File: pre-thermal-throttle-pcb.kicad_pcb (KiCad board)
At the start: 2 copper layers, 101.6 x 89.5 mm, 62 parts, among them IC1 LMR51420XFDDCR, IC2 ADR02BRZ-REEL7, IC3 ADR02BRZ-REEL7, IC4 ADR02BRZ-REEL7, IC5 ADR02BRZ-REEL7, J1 RJHSE-5381-ND, J2 STEERING, J3 Motor Throttle Connector, U1 SN65HVD230, U2 BMI088, U3 MAX3485CSA, U4 MCP3008, U5 ESP32-DevKitC

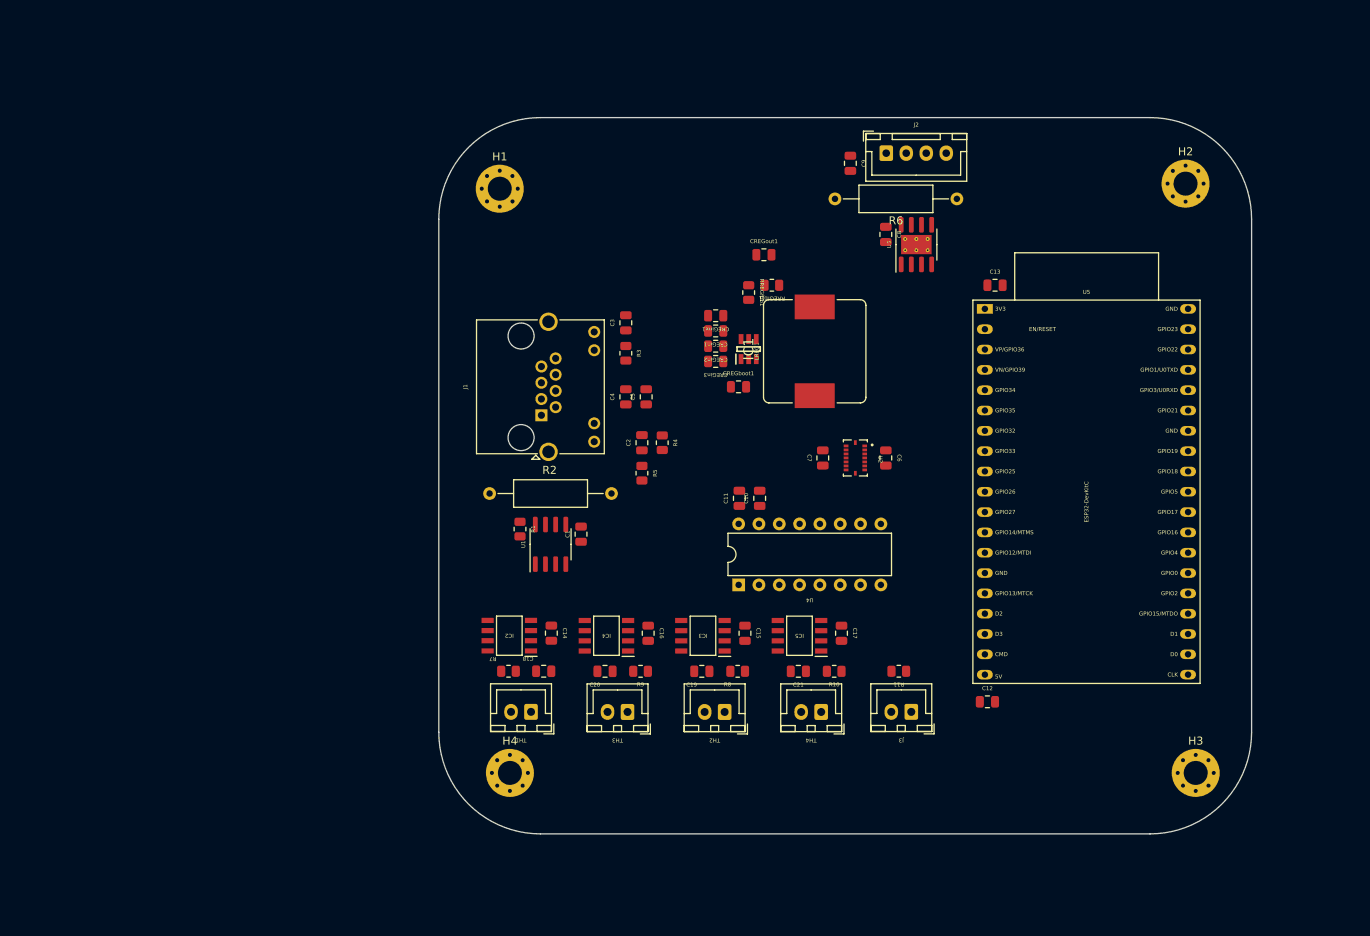
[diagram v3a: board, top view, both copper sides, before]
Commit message: Add extra rj45 for CAN splice and connect imu ints
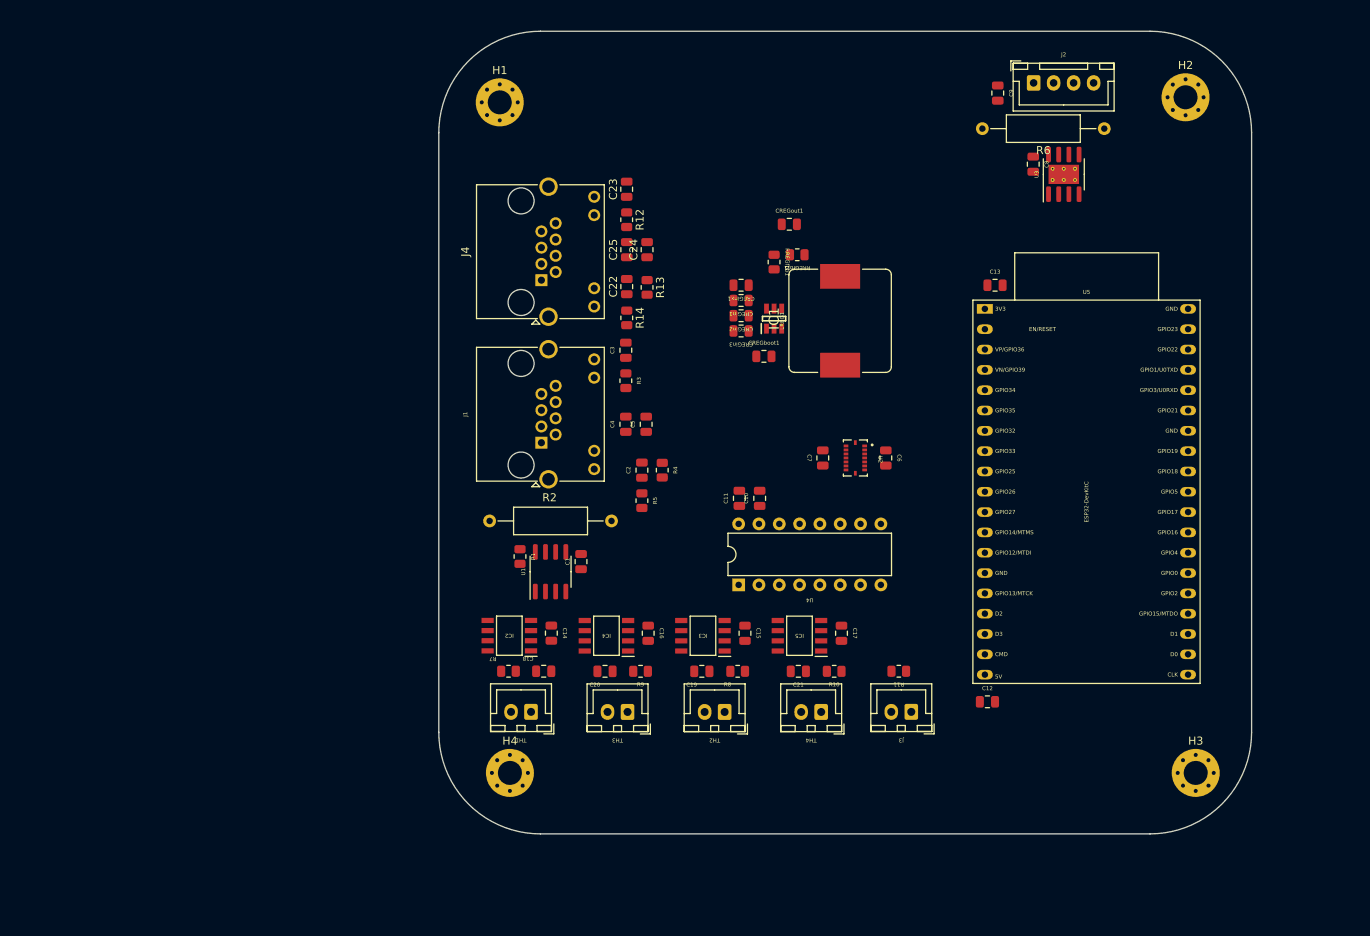
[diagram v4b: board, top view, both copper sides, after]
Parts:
- added C22: 100 nF, Capacitor_SMD:C_0805_2012Metric, F.Cu at (156.8, 69.4)
- added C23: 100 nF, Capacitor_SMD:C_0805_2012Metric, F.Cu at (156.8, 57.2)
- added C24: 100 nF, Capacitor_SMD:C_0805_2012Metric, F.Cu at (159.4, 64.8)
- added C25: 100 nF, Capacitor_SMD:C_0805_2012Metric, F.Cu at (156.8, 64.8)
- added J4: RJHSE-5381-ND, Connector_RJ:RJ45_Amphenol_RJHSE538X, F.Cu at (146.2, 68.6)
- added R12: 130R, Resistor_SMD:R_0805_2012Metric, F.Cu at (156.8, 61.0)
- added R13: 10K, Resistor_SMD:R_0805_2012Metric, F.Cu at (159.4, 69.5)
- added R14: 130R, Resistor_SMD:R_0805_2012Metric, F.Cu at (156.8, 73.3)
- moved C8 20.4 mm to (207.7, 54.1)
- moved C9 20.4 mm to (203.2, 45.2)
- moved J2 20.4 mm to (207.7, 43.9)
- moved U3 20.4 mm to (211.5, 55.4)
- moved R6 20.4 mm to (216.5, 49.6)
- moved H1 10.8 mm to (141.0, 46.4)
- moved H2 10.8 mm to (226.7, 45.7)
- moved CREGboot1 4.96 mm to (174.0, 78.1)
- moved RREGfbt1 4.96 mm to (178.2, 65.4)
- moved CREGin1 4.96 mm to (171.1, 71.1)
- moved CREGinx1 4.96 mm to (171.1, 69.2)
- moved CREGout1 4.96 mm to (177.2, 61.6)
- moved LREG1 4.96 mm to (183.5, 73.7)
- moved RREGfbb1 4.96 mm to (175.3, 66.3)
- moved CREGin2 4.96 mm to (171.1, 73.0)
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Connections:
- U2 pad 13: unconnected-(U2-Pad13) -> IMU_INT2
- U2 pad 16: unconnected-(U2-Pad16) -> IMU_INT1
- U5 pad 21: unconnected-(U5-Pad21) -> IMU_INT1
- U5 pad 22: unconnected-(U5-Pad22) -> IMU_INT2
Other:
- board size 101.6 x 89.5 mm -> 101.6 x 100.3 mm

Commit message: Finish most traces
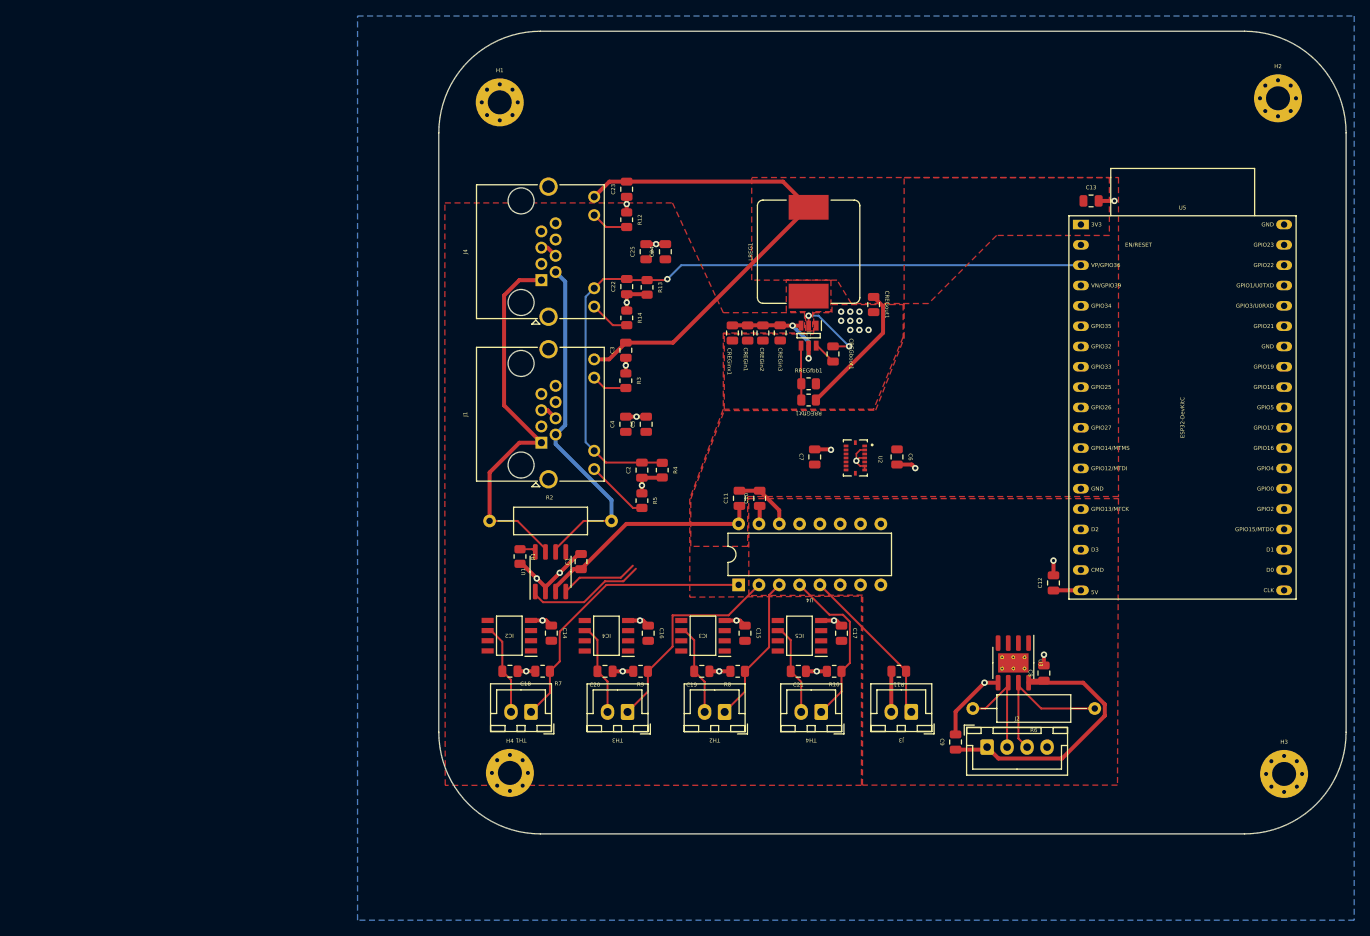
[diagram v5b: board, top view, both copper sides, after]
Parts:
- moved J2 83.2 mm to (201.9, 126.9)
- moved C9 81.3 mm to (197.9, 126.3), turned to 90 degrees
- moved R6 72.5 mm to (215.3, 122.1)
- moved C8 63.6 mm to (209.0, 117.7), turned to 90 degrees
- moved U3 61.4 mm to (205.2, 116.4), turned to -90 degrees
- moved RREGfbt1 18.2 mm to (179.6, 83.6)
- moved C12 17.0 mm to (210.2, 106.4), turned to 90 degrees
- moved C13 16.0 mm to (214.9, 58.7)
- moved U5 16.0 mm to (213.6, 61.6)
- moved RREGfbb1 15.8 mm to (179.6, 81.5), turned to 0 degrees
- moved CREGout1 14.6 mm to (187.7, 71.6), turned to -90 degrees
- moved H2 11.6 mm to (238.3, 45.8)
- moved H3 11.0 mm to (239.0, 130.3)
- moved LREG1 9.49 mm to (179.6, 65.0)
- moved CREGboot1 8.64 mm to (182.6, 77.8), turned to 90 degrees
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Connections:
- R10 pad 1: ADC_CH4 -> ADC_CH3
- TH4 pad 1: ADC_CH4 -> ADC_CH3
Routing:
- net +3.3V: track 0.00 -> 109.4 mm
- net ESP_OK_LED: track 0.00 -> 92.5 mm, vias 0 -> 1
- net GND: track 0.00 -> 88.4 mm, vias 0 -> 32
- net CAR_CANH: track 0.00 -> 48.7 mm
- net CAR_CANL: track 0.00 -> 43.8 mm
- net +5V: track 0.00 -> 41.4 mm
- net ADC_CH0: track 0.00 -> 36.3 mm
- net ADC_CH1: track 0.00 -> 26.8 mm
- net ADC_CH3: track 0.00 -> 21.0 mm
- net THROTTLE_SIG: track 0.00 -> 20.6 mm
- net STEERING_B: track 0.00 -> 19.6 mm
- net +12V: track 0.00 -> 19.5 mm, vias 0 -> 2
- net ADC_CH2: track 0.00 -> 18.7 mm
- net CAN_TXD: track 0.00 -> 15.1 mm
- net STEERING_A: track 0.00 -> 14.1 mm
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- added copper zone on F.Cu, net +12V
- added copper zone on F.Cu, net +3.3V
- added copper zone on F.Cu, net +5V
- added copper zone on B.Cu, net GND
- added copper zone on F.Cu, net GND
- added copper zone on F.Cu, net Net-(CREGboot1-Pad2)
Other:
- board size 101.6 x 100.3 mm -> 113.4 x 100.3 mm

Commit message: Hopefully finished?
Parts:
- moved H2 3.34 mm to (237.7, 49.1)
- moved H1 3.07 mm to (142.2, 49.1)
- moved H3 1.27 mm to (237.7, 130.3)
- moved CREGin2 0.13 mm to (174.0, 75.2)
- moved CREGinx1 0.13 mm to (169.9, 75.2)
- moved H4 0.13 mm to (142.2, 130.3)
- renumbered IC4 to IC3, IC3 to IC4, TH3 to TH2, TH2 to TH3
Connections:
- U5 pad 12: unconnected-(U5-Pad12) -> ESP ADC CS
- U5 pad 15: unconnected-(U5-Pad15) -> RS485 RTS
- U5 pad 21: IMU_INT1 -> unconnected-(U5-Pad21)
- U5 pad 22: IMU_INT2 -> unconnected-(U5-Pad22)
- U5 pad 23: unconnected-(U5-Pad23) -> ESP_OK_LED
- U5 pad 3: ESP_OK_LED -> unconnected-(U5-Pad3)
- U5 pad 4: ESP ADC CS -> unconnected-(U5-Pad4)
- U5 pad 5: RS485 RTS -> unconnected-(U5-Pad5)
- U5 pad 7: unconnected-(U5-Pad7) -> IMU_INT2
- U5 pad 8: unconnected-(U5-Pad8) -> IMU_INT1
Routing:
- net ESP CIPO: track 0.00 -> 77.8 mm, vias 0 -> 1
- net ESP COPI: track 0.00 -> 76.3 mm, vias 0 -> 1
- net ESP SPI CLK: track 0.00 -> 72.2 mm
- net CAN_TXD: track 15.1 -> 85.8 mm, vias 0 -> 1
- net ESP Gyro CS: track 0.00 -> 69.2 mm
- net CAN_RXD: track 9.72 -> 78.1 mm, vias 0 -> 1
- net ESP Accel : track 0.00 -> 63.0 mm
- net TXD2: track 0.00 -> 51.7 mm
- net RXD2: track 0.00 -> 48.9 mm
- net IMU_INT2: track 0.00 -> 37.9 mm
- net ESP_OK_LED: track 92.5 -> 126.6 mm
- net IMU_INT1: track 0.00 -> 32.9 mm
- net ESP ADC CS: track 0.00 -> 31.7 mm
- net RS485 RTS: track 0.00 -> 21.9 mm
- net +3.3V: track 109.4 -> 122.4 mm, vias 0 -> 2
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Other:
- board size 113.4 x 100.3 mm -> 113.1 x 98.8 mm
- board text added: "3.3->12V Regulator"
- board text added: "5V"
- board text added: "A"
- board text added: "ADC"
- board text added: "B"
- board text added: "BMI088 IMU"
- board text added: "CAN Transceiver"
- board text added: "ESP32 MCU"
- board text added: "GND"
- board text added: "RJ45 12V+CAN"
- board text added: "RS485"
- board text added: "SIG"
- board text added: "Thermistors"

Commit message: Muh silkscreen
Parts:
- added G1: LOGO, pre_logo:pre_logo_medium, F.Cu at (212.5, 48.3)
- added G2: LOGO, pre_logo:pre_logo_big, B.Cu at (189.1, 90.9)
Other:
- board text added: "81.15mm"
- board text added: "95.5mm"
- board text added: "M3 SCREW"
- board text added: "PRINCETON RACING ELECTRIC VCU BOARD 2022-2023 SEASON"
